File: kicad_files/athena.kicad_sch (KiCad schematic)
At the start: 244 parts, among them J1 SM04B-SRSS-TB(LF)(SN), J2 TYPE-C-31-M12, J3 SM04B-SRSS-TB(LF)(SN), J4 ARM JTAG, J5 EXTRA PINS, Q1 DTC123JKAT146, SW1 MX Switch, SW10 MX Switch, SW100 MX Switch, SW101 MX Switch, SW102 MX Switch, SW103 MX Switch, SW104 MX Switch, SW105 MX Switch, SW106 MX Switch, SW107 MX Switch, SW108 MX Switch, SW109 MX Switch, SW11 MX Switch, SW110 MX Switch, SW111 MX Switch, SW112 MX Switch, SW113 K2-1187SQ-A4SW-06, SW12 MX Switch, SW13 MX Switch, SW14 MX Switch, SW15 MX Switch, SW16 MX Switch, SW17 MX Switch, SW18 MX Switch, SW19 MX Switch, SW2 MX Switch, SW20 MX Switch, SW21 MX Switch, SW22 MX Switch, SW23 MX Switch, SW24 MX Switch, SW25 MX Switch, SW26 MX Switch, SW27 MX Switch, SW28 MX Switch, SW29 MX Switch, SW3 MX Switch, SW30 MX Switch, SW31 MX Switch, SW32 MX Switch, SW33 MX Switch, SW34 MX Switch, SW35 MX Switch, SW36 MX Switch, SW37 MX Switch, SW38 MX Switch, SW39 MX Switch, SW4 MX Switch, SW40 MX Switch, SW41 MX Switch, SW42 MX Switch, SW43 MX Switch, SW44 MX Switch, SW45 MX Switch, SW46 MX Switch, SW47 MX Switch, SW48 MX Switch, SW49 MX Switch, SW5 MX Switch, SW50 MX Switch, SW51 MX Switch, SW52 MX Switch, SW53 MX Switch, SW54 MX Switch, SW55 MX Switch, SW56 MX Switch, SW57 MX Switch, SW58 MX Switch, SW59 MX Switch, SW6 MX Switch, SW60 MX Switch, SW61 MX Switch, SW62 MX Switch, SW63 MX Switch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

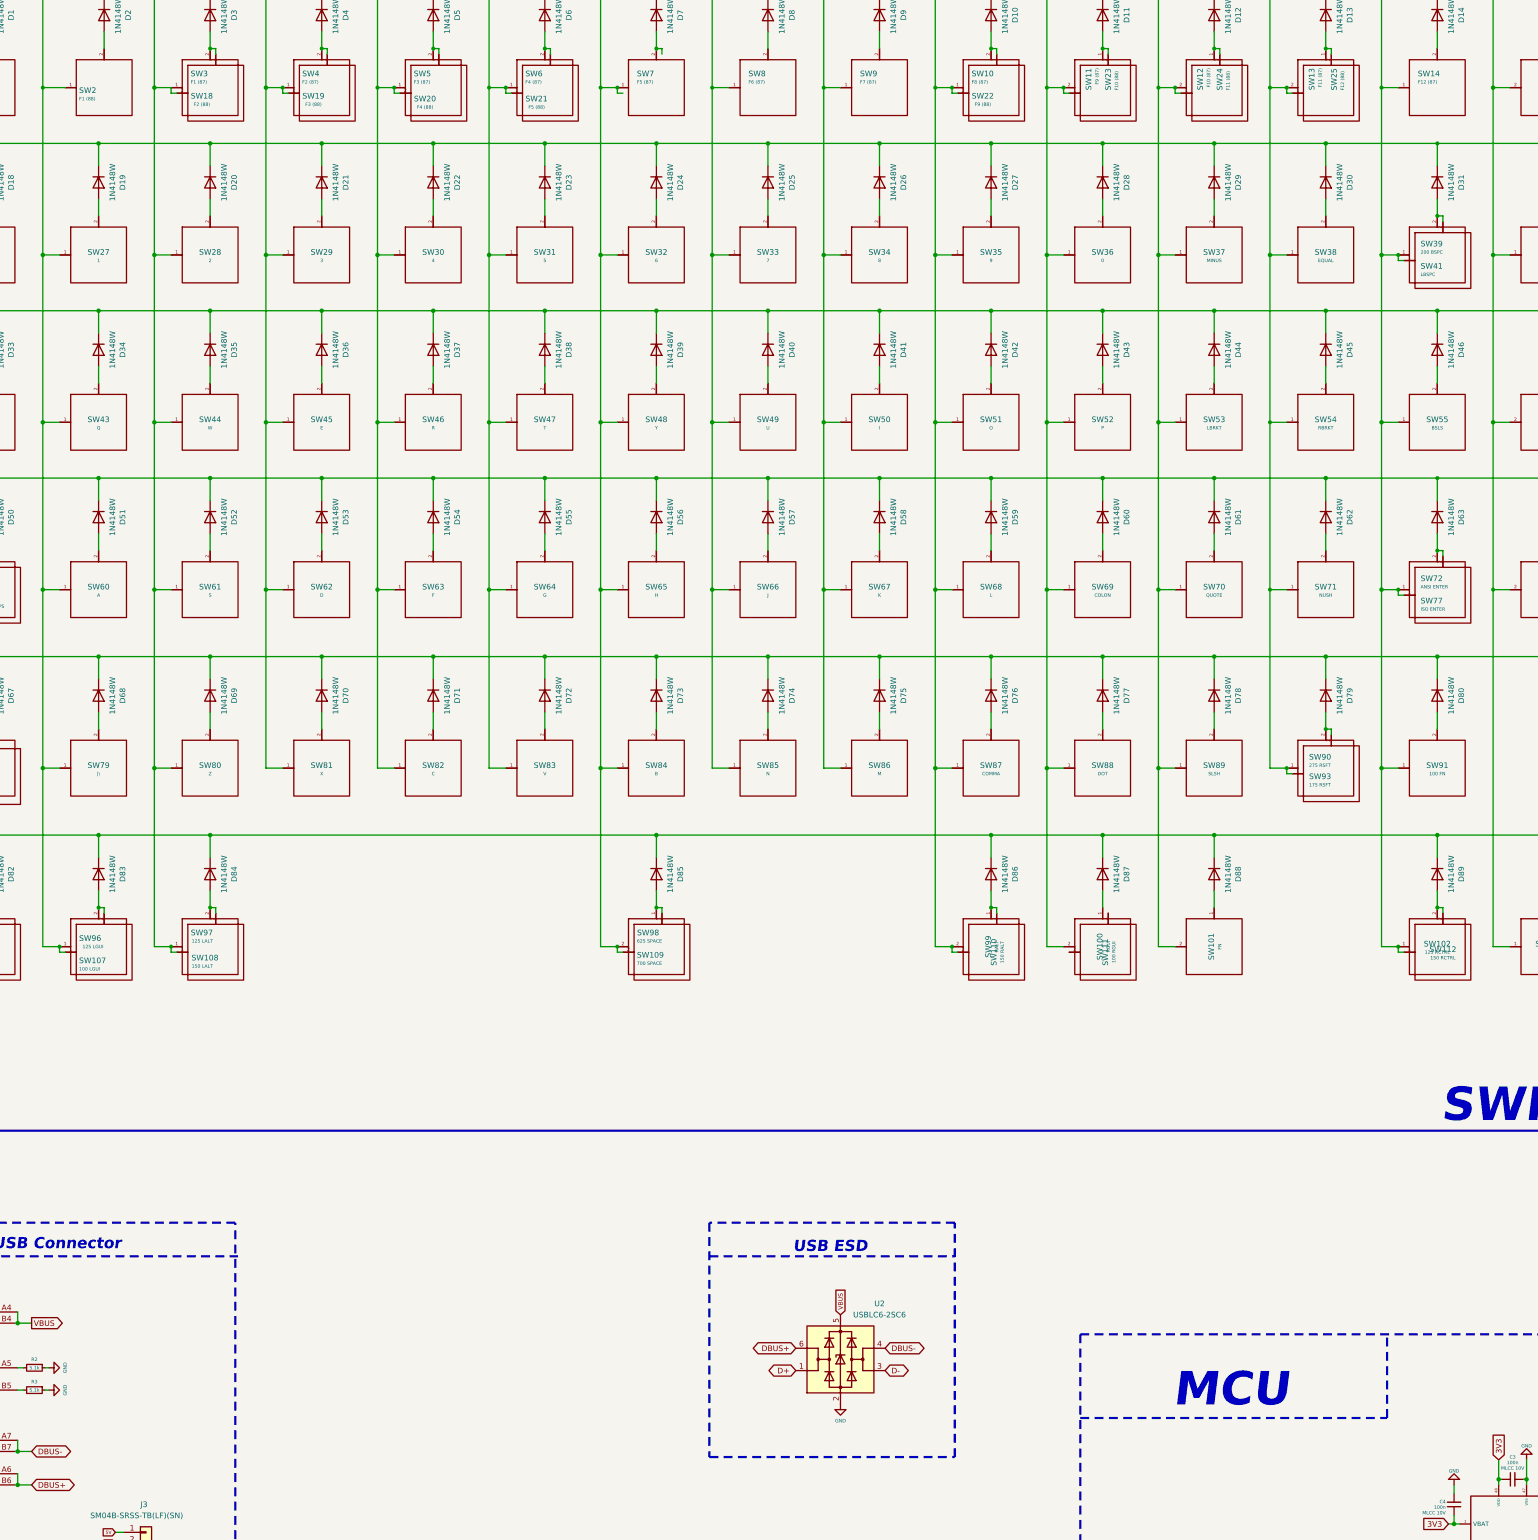
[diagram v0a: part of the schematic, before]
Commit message: Added Athena logo
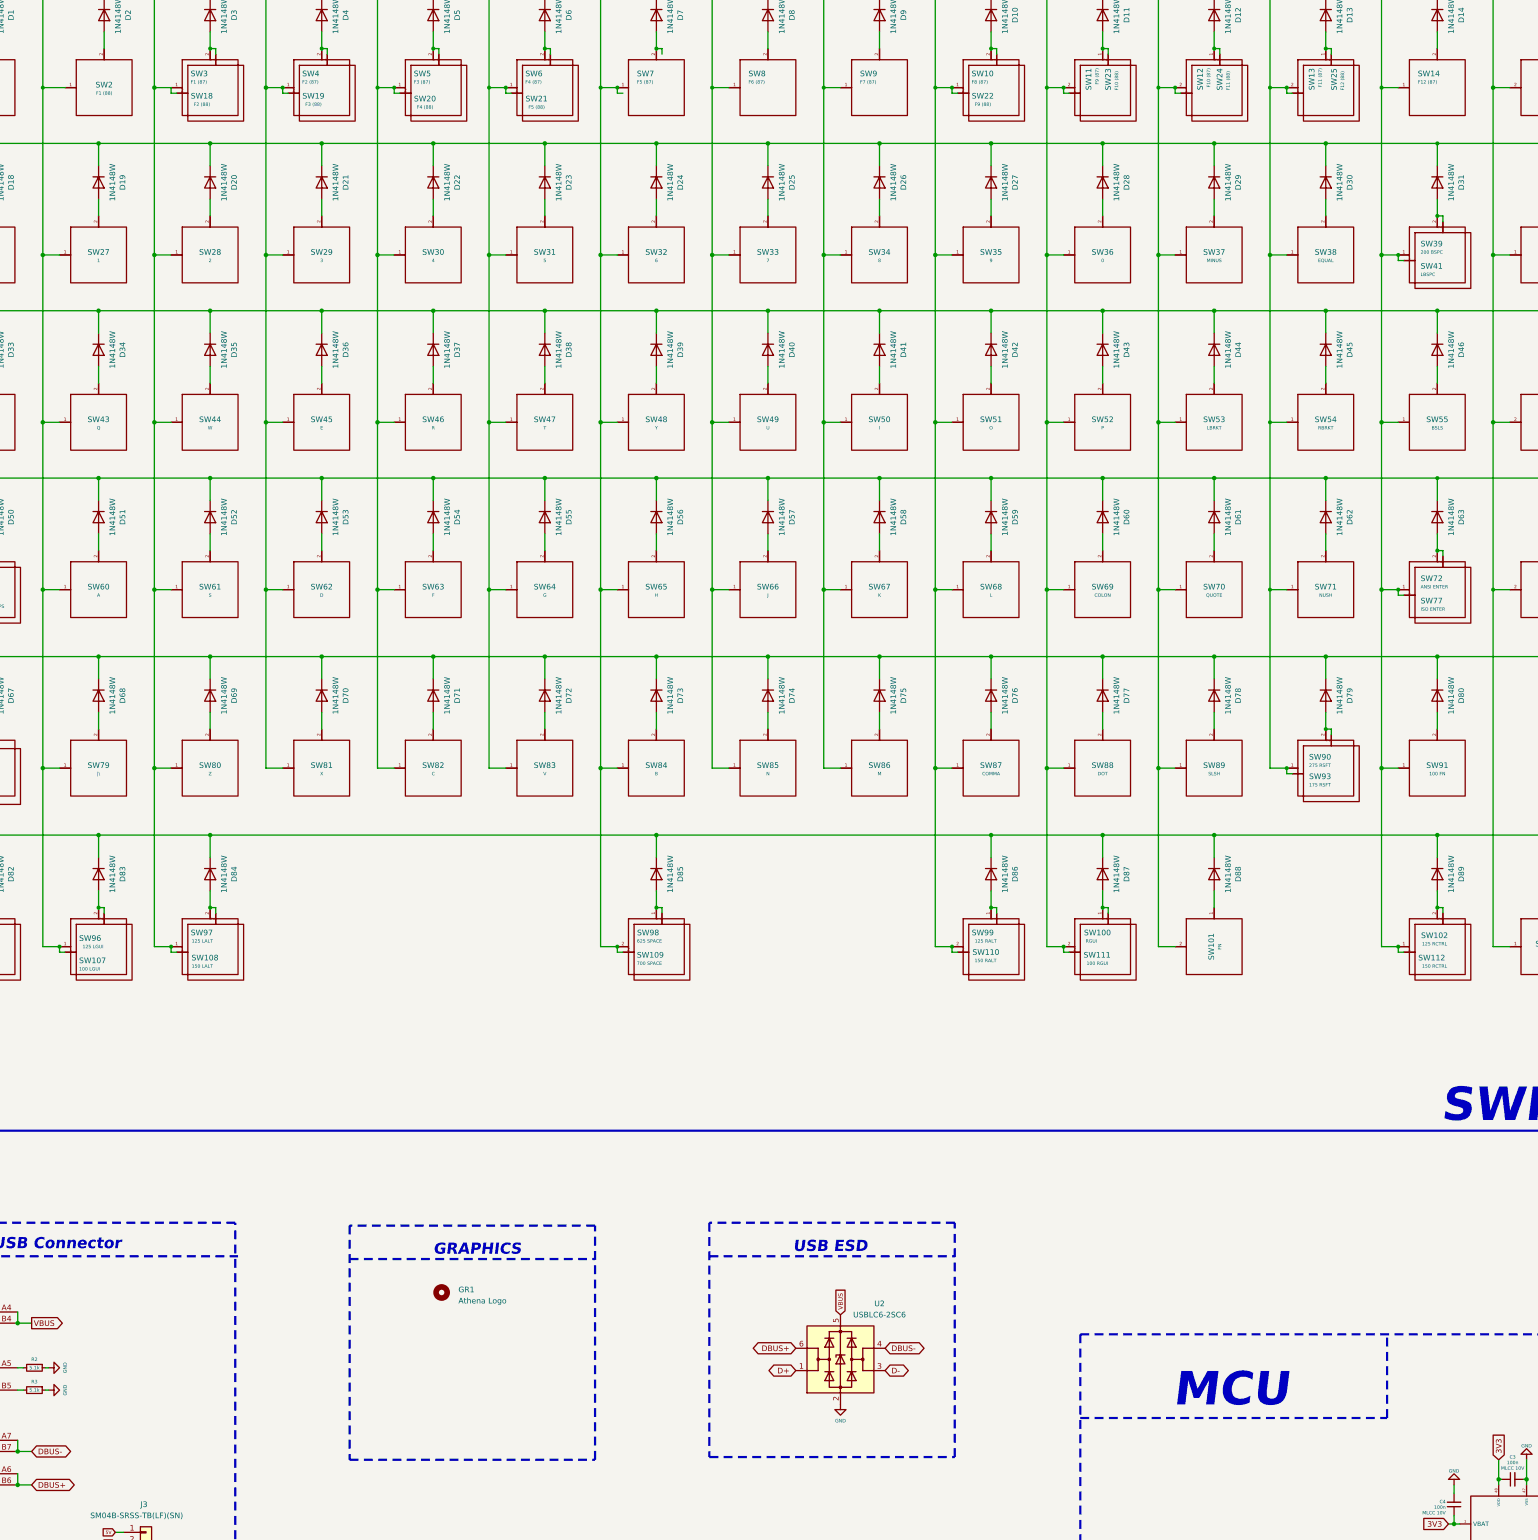
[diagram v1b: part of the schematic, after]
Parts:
- added GR1: Athena Logo, athena_library:athena_logo_100mm, symbol Mechanical:MountingHole
- SW99: Keycode RALT -> 125 RALT
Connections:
- net C10: now also SW111.2
- net at SW111.1: now also D87.2 (A), SW100.1
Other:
- note added: "GRAPHICS"
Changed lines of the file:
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@@
     (title "Athena PCB schematic")
     (date "2021-05-06")
-    (rev "V0.1")
+    (rev "V0.2")
     (company "Acheron Project")
     (comment 1 "Designed by Gondolindrim")
@@
   (junction (at 296.545 236.22) (diameter 1.016) (color 0 0 0 0))
   (junction (at 300.355 81.28) (diameter 0.9144) (color 0 0 0 0))
+  (junction (at 300.355 276.86) (diameter 0.9144) (color 0 0 0 0))
   (junction (at 309.245 55.88) (diameter 1.016) (color 0 0 0 0))
   (junction (at 309.245 72.39) (diameter 0.9144) (color 0 0 0 0))
@@
   (junction (at 309.245 210.82) (diameter 1.016) (color 0 0 0 0))
   (junction (at 309.245 251.46) (diameter 1.016) (color 0 0 0 0))
+  (junction (at 309.245 267.97) (diameter 0.9144) (color 0 0 0 0))
   (junction (at 321.945 81.28) (diameter 0.9144) (color 0 0 0 0))
   (junction (at 321.945 119.38) (diameter 1.016) (color 0 0 0 0))
@@
     (stroke (width 0) (type solid) (color 0 0 0 0))
   )
+  (wire (pts (xy 300.355 278.13) (xy 300.355 276.86))
+    (stroke (width 0) (type solid) (color 0 0 0 0))
+  )
   (wire (pts (xy 301.625 82.55) (xy 300.355 82.55))
     (stroke (width 0) (type solid) (color 0 0 0 0))
   )
+  (wire (pts (xy 301.625 278.13) (xy 300.355 278.13))
+    (stroke (width 0) (type solid) (color 0 0 0 0))
+  )
   (wire (pts (xy 309.245 55.88) (xy 283.845 55.88))
     (stroke (width 0) (type solid) (color 0 0 0 0))
@@
     (stroke (width 0) (type solid) (color 0 0 0 0))
   )
+  (wire (pts (xy 309.245 267.97) (xy 310.515 267.97))
+    (stroke (width 0) (type solid) (color 0 0 0 0))
+  )
   (wire (pts (xy 310.515 72.39) (xy 309.245 72.39))
     (stroke (width 0) (type solid) (color 0 0 0 0))
@@
     (stroke (width 0) (type solid) (color 0 0 0 0))
   )
+  (wire (pts (xy 310.515 269.24) (xy 310.515 267.97))
+    (stroke (width 0) (type solid) (color 0 0 0 0))
+  )
   (wire (pts (xy 321.945 43.18) (xy 321.945 81.28))
     (stroke (width 0) (type solid) (color 0 0 0 0))
@@
     (stroke (width 0.508) (type dash) (color 0 0 0 0))
   )
+  (polyline (pts (xy 137.795 340.36) (xy 137.795 393.7))
+    (stroke (width 0.508) (type dash) (color 0 0 0 0))
+  )
+  (polyline (pts (xy 137.795 347.98) (xy 193.675 347.98))
+    (stroke (width 0.508) (type dash) (color 0 0 0 0))
+  )
+  (polyline (pts (xy 137.795 393.7) (xy 193.675 393.7))
+    (stroke (width 0.508) (type dash) (color 0 0 0 0))
+  )
+  (polyline (pts (xy 193.675 340.36) (xy 137.795 340.36))
+    (stroke (width 0.508) (type dash) (color 0 0 0 0))
+  )
+  (polyline (pts (xy 193.675 393.7) (xy 193.675 340.36))
+    (stroke (width 0.508) (type dash) (color 0 0 0 0))
+  )
   (polyline (pts (xy 219.71 339.725) (xy 219.71 393.065))
     (stroke (width 0.508) (type dash) (color 0 0 0 0))
@@
     (effects (font (size 2.54 2.54) (thickness 0.508) bold italic) (justify left bottom))
   )
+  (text "GRAPHICS" (at 156.845 347.345 0)
+    (effects (font (size 2.54 2.54) (thickness 0.508) bold italic) (justify left bottom))
+  )
   (text "USB ESD" (at 238.76 346.71 0)
     (effects (font (size 2.54 2.54) (thickness 0.508) bold italic) (justify left bottom))
@@
     (pin "2")
   )
+  (symbol (lib_id "Mechanical:MountingHole") (at 158.75 355.6 0) (unit 1)
+    (in_bom no) (on_board yes) (fields_autoplaced)
+    (property "Reference" "GR1" (id 0) (at 162.56 354.9649 0)
+      (effects (font (size 1.27 1.27)) (justify left))
+    )
+    (property "Value" "Athena Logo" (id 1) (at 162.56 357.5049 0)
+      (effects (font (size 1.27 1.27)) (justify left))
+    )
+    (property "Footprint" "athena_library:athena_logo_100mm" (id 2) (at 158.75 355.6 0)
+      (effects (font (size 1.27 1.27)) hide)
+    )
+    (property "Datasheet" "~" (id 3) (at 158.75 355.6 0)
+      (effects (font (size 1.27 1.27)) hide)
+    )
+  )
   (symbol (lib_id "Device:Fuse") (at 556.26 454.025 90) (unit 1)
     (in_bom yes) (on_board yes)
@@
   (symbol (lib_id "acheronSymbols:Mechanical_Switch") (at 81.915 81.28 0) (unit 1)
     (in_bom yes) (on_board yes)
-    (property "Reference" "SW2" (id 0) (at 76.2 81.915 0)
-      (effects (font (size 1.27 1.27)) (justify left))
-    )
+    (property "Reference" "SW2" (id 0) (at 81.915 80.645 0))
     (property "Value" "MX Switch" (id 1) (at 81.915 85.09 0)
       (effects (font (size 0.762 0.762)) hide)
@@
       (effects (font (size 1.27 1.27)) hide)
     )
-    (property "Keycode" "F1 (88)" (id 7) (at 76.2 83.82 0)
-      (effects (font (size 0.762 0.762)) (justify left))
+    (property "Keycode" "F1 (88)" (id 7) (at 81.915 82.55 0)
+      (effects (font (size 0.762 0.762)))
     )
     (property "Manufacturer" "Kaihua" (id 8) (at 81.915 81.28 0)
@@
   (symbol (lib_id "acheronSymbols:Mechanical_Switch") (at 283.845 276.86 90) (mirror x) (unit 1)
     (in_bom yes) (on_board yes)
-    (property "Reference" "SW99" (id 0) (at 283.21 276.86 0))
+    (property "Reference" "SW99" (id 0) (at 284.48 273.685 90)
+      (effects (font (size 1.27 1.27)) (justify left))
+    )
     (property "Value" "MX Switch" (id 1) (at 287.655 276.86 0)
       (effects (font (size 0.762 0.762)) hide)
@@
       (effects (font (size 1.27 1.27)) hide)
     )
-    (property "Keycode" "RALT" (id 7) (at 285.115 276.86 0)
-      (effects (font (size 0.762 0.762)))
+    (property "Keycode" "125 RALT" (id 7) (at 285.115 275.59 90)
+      (effects (font (size 0.762 0.762)) (justify left))
     )
     (property "Manufacturer" "Kaihua" (id 8) (at 283.845 276.86 0)
@@
   (symbol (lib_id "acheronSymbols:Mechanical_Switch") (at 285.115 278.13 90) (mirror x) (unit 1)
     (in_bom yes) (on_board yes)
-    (property "Reference" "SW110" (id 0) (at 284.48 278.13 0))
+    (property "Reference" "SW110" (id 0) (at 285.75 278.13 90)
+      (effects (font (size 1.27 1.27)) (justify left))
+    )
     (property "Value" "MX Switch" (id 1) (at 288.925 278.13 0)
       (effects (font (size 0.762 0.762)) hide)
@@
       (effects (font (size 1.27 1.27)) hide)
     )
-    (property "Keycode" "150 RALT" (id 7) (at 286.385 278.13 0)
+    (property "Keycode" "150 RALT" (id 7) (at 282.575 280.035 90)
       (effects (font (size 0.762 0.762)))
     )
@@
   (symbol (lib_id "acheronSymbols:Mechanical_Switch") (at 309.245 276.86 90) (mirror x) (unit 1)
     (in_bom yes) (on_board yes)
-    (property "Reference" "SW100" (id 0) (at 308.61 276.86 0))
+    (property "Reference" "SW100" (id 0) (at 311.15 273.685 90)
+      (effects (font (size 1.27 1.27)) (justify left))
+    )
     (property "Value" "MX Switch" (id 1) (at 313.055 276.86 0)
       (effects (font (size 0.762 0.762)) hide)
@@
       (effects (font (size 1.27 1.27)) hide)
     )
-    (property "Keycode" "RGUI" (id 7) (at 310.515 276.86 0)
-      (effects (font (size 0.762 0.762)))
+    (property "Keycode" "RGUI" (id 7) (at 307.975 275.59 90)
+      (effects (font (size 0.762 0.762)) (justify left))
     )
     (property "Manufacturer" "Kaihua" (id 8) (at 309.245 276.86 0)
@@
   (symbol (lib_id "acheronSymbols:Mechanical_Switch") (at 310.515 278.13 90) (mirror x) (unit 1)
     (in_bom yes) (on_board yes)
-    (property "Reference" "SW111" (id 0) (at 309.88 278.13 0))
+    (property "Reference" "SW111" (id 0) (at 307.975 278.765 90))
     (property "Value" "MX Switch" (id 1) (at 314.325 278.13 0)
       (effects (font (size 0.762 0.762)) hide)
@@
       (effects (font (size 1.27 1.27)) hide)
     )
-    (property "Keycode" "100 RGUI" (id 7) (at 311.785 278.13 0)
-      (effects (font (size 0.762 0.762)))
+    (property "Keycode" "100 RGUI" (id 7) (at 310.515 280.67 90)
+      (effects (font (size 0.762 0.762)) (justify left))
     )
     (property "Manufacturer" "Kaihua" (id 8) (at 310.515 278.13 0)
@@
   (symbol (lib_id "acheronSymbols:Mechanical_Switch") (at 385.445 276.86 0) (unit 1)
     (in_bom yes) (on_board yes)
-    (property "Reference" "SW102" (id 0) (at 385.445 276.225 0))
+    (property "Reference" "SW102" (id 0) (at 384.81 274.32 0))
     (property "Value" "MX Switch" (id 1) (at 385.445 280.67 0)
       (effects (font (size 0.762 0.762)) hide)
@@
       (effects (font (size 1.27 1.27)) hide)
     )
-    (property "Keycode" "125 RCTRL" (id 7) (at 385.445 278.13 0)
+    (property "Keycode" "125 RCTRL" (id 7) (at 384.81 276.225 0)
       (effects (font (size 0.762 0.762)))
     )
@@
   (symbol (lib_id "acheronSymbols:Mechanical_Switch") (at 386.715 278.13 0) (unit 1)
     (in_bom yes) (on_board yes)
-    (property "Reference" "SW112" (id 0) (at 386.715 277.495 0))
+    (property "Reference" "SW112" (id 0) (at 384.175 279.4 0))
     (property "Value" "MX Switch" (id 1) (at 386.715 281.94 0)
       (effects (font (size 0.762 0.762)) hide)
@@
       (effects (font (size 1.27 1.27)) hide)
     )
-    (property "Keycode" "150 RCTRL" (id 7) (at 386.715 279.4 0)
+    (property "Keycode" "150 RCTRL" (id 7) (at 384.81 281.305 0)
       (effects (font (size 0.762 0.762)))
     )
@@
       (reference "FB1") (unit 1) (value "CBW201209U121T") (footprint "Inductor_SMD:L_0805_2012Metric")
     )
+    (path "/32aba6eb-a8c1-43c4-9a0a-ec70aeac5095"
+      (reference "GR1") (unit 1) (value "Athena Logo") (footprint "athena_library:athena_logo_100mm")
+    )
     (path "/fbe34ab1-2e19-41e5-b9bd-a3c174c23a41"
